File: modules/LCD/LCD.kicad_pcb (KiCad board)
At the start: 2 copper layers, 82.5 x 40.6 mm, 15 parts, among them J1 Conn_01x10_Male, J2 Conn_01x10_Male, J3 Conn_01x03_Male, J4 Conn_01x03_Male, U1 74LS139

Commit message: LCD. Fix hash.
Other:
- board text added: "e0b295"
- board text removed: "1c146a"

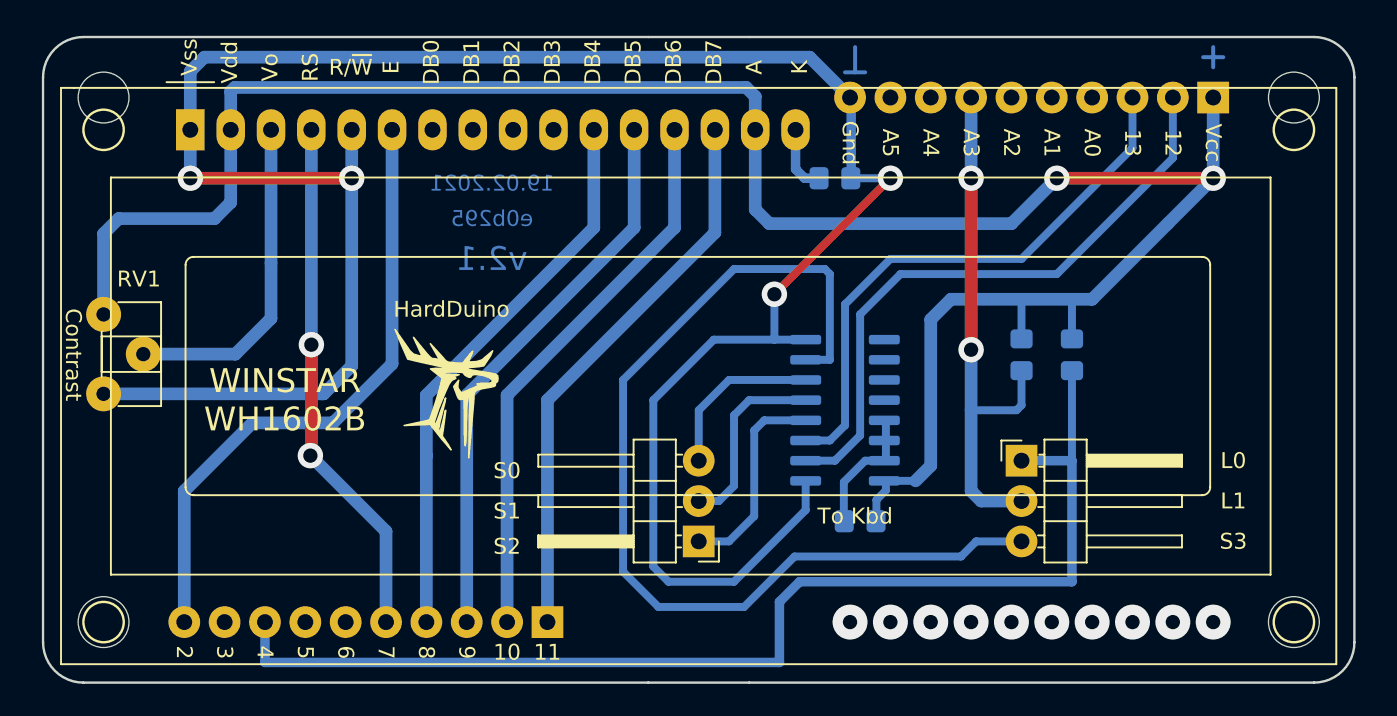
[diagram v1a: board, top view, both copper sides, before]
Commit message: LCD. Fix grid to 2.54, fix mounting holes position. This version is uncompatible with previous!!
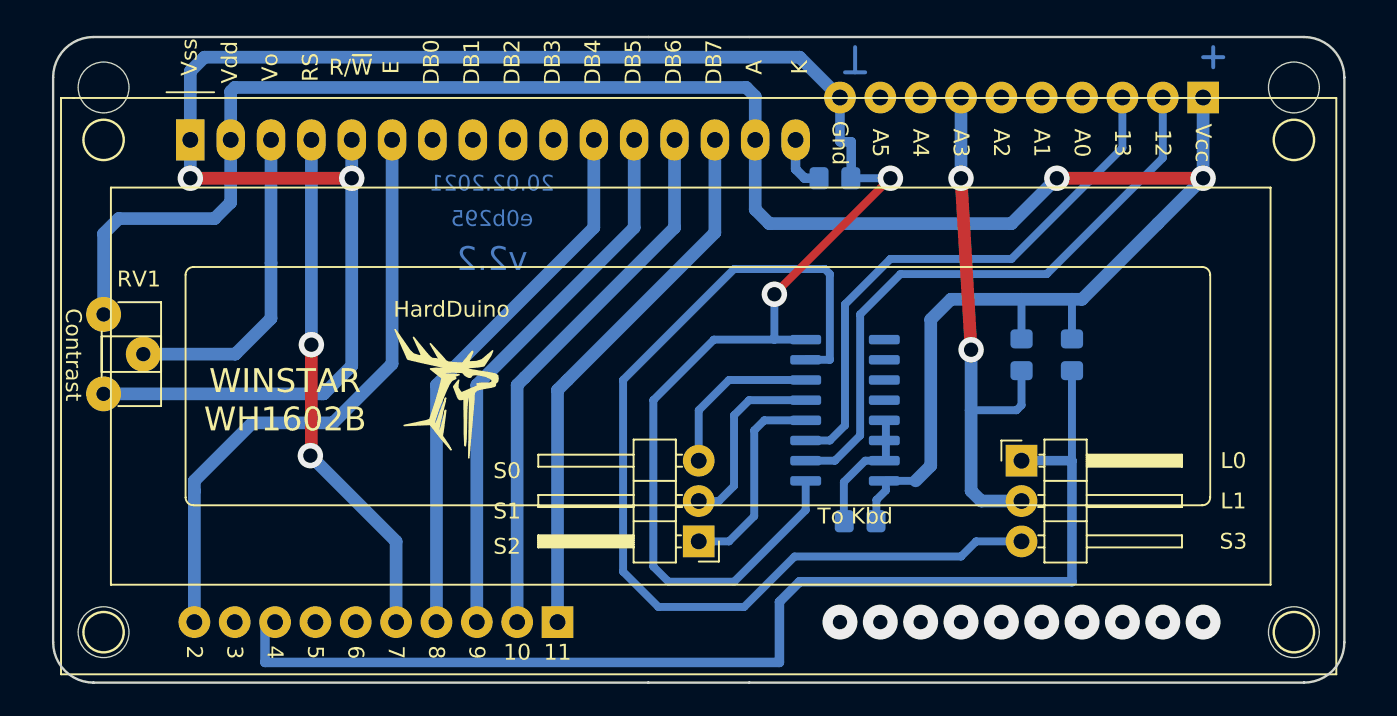
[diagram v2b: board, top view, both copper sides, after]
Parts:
- moved H1 0.64 mm to (148.0, 62.9)
- moved H3 0.64 mm to (73.0, 62.9)
- moved H2 0.64 mm to (148.0, 28.6)
- moved H4 0.64 mm to (73.0, 28.6)
- moved DS1 0.63 mm to (78.5, 31.9)
- moved J1 0.63 mm to (142.2, 29.2)
- moved J2 0.63 mm to (101.6, 62.2)
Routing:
- net VCC: track 138.5 -> 136.9 mm
- net /12: track 39.3 -> 38.6 mm
- net /13: track 35.8 -> 35.2 mm
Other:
- board size 82.5 x 40.6 mm -> 81.3 x 40.6 mm
- board text added: "20.02.2021"
- board text added: "v2.2"
- board text removed: "19.02.2021"
- board text removed: "v2.1"

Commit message: Now 2x shields have distance between 1x parts
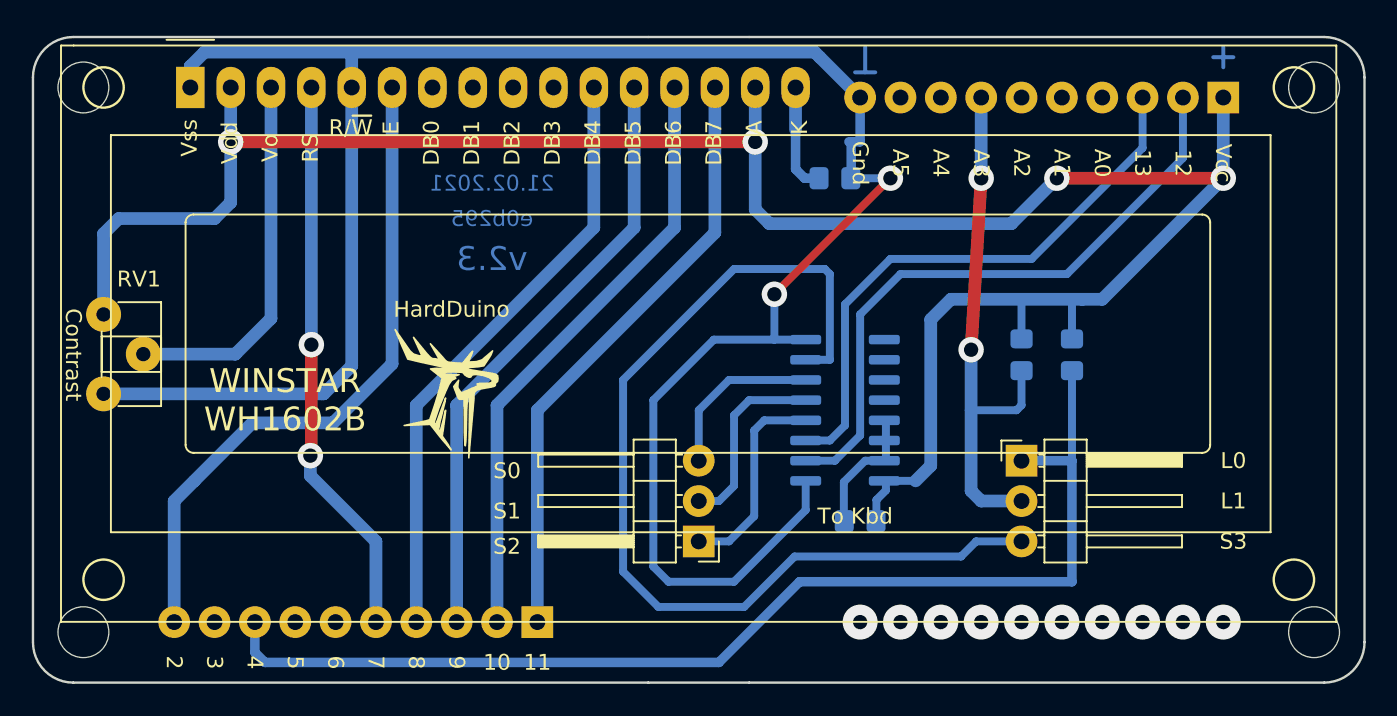
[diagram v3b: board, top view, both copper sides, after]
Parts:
- moved DS1 3.30 mm to (78.5, 28.6)
- moved H3 1.27 mm to (71.8, 62.9)
- moved H4 1.27 mm to (71.8, 28.6)
- moved J2 1.27 mm to (100.3, 62.2)
- moved H1 1.27 mm to (149.2, 62.9)
- moved H2 1.27 mm to (149.2, 28.6)
- moved J1 1.27 mm to (143.5, 29.2)
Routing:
- net GND: track 147.1 -> 139.2 mm, vias 4 -> 2
- net /8: track 35.1 -> 38.3 mm
- net /2: track 39.1 -> 42.3 mm
- net /11: track 35.1 -> 38.3 mm
- net /9: track 35.1 -> 38.3 mm
- net /10: track 35.1 -> 38.3 mm
- net VCC: track 136.9 -> 139.7 mm, vias 2 -> 4
- net Net-(DS1-Pad3): track 20.8 -> 23.5 mm
- net Net-(DS1-Pad16): track 4.16 -> 6.83 mm
- net /7: track 33.2 -> 35.4 mm
- net /4: track 74.1 -> 72.2 mm
- net /13: track 35.2 -> 36.5 mm
- net /12: track 38.6 -> 39.9 mm
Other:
- board size 81.3 x 40.6 mm -> 83.8 x 40.6 mm
- board text added: "21.02.2021"
- board text added: "v2.3"
- board text removed: "20.02.2021"
- board text removed: "v2.2"

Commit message: LCD. Pot was moved.
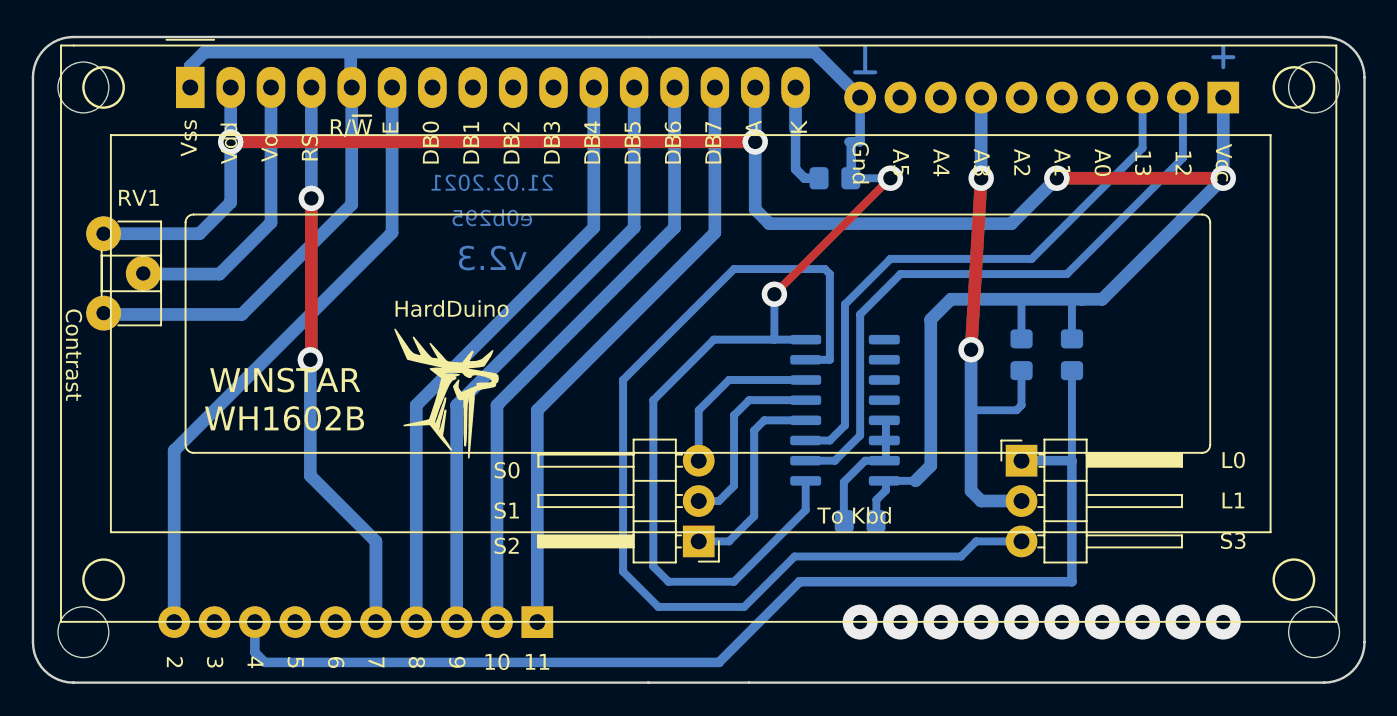
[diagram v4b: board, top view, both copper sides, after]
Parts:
- moved RV1 5.08 mm to (73.0, 37.8)
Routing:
- net GND: track 139.2 -> 131.2 mm
- net Net-(DS1-Pad3): track 23.5 -> 17.9 mm
- net VCC: track 139.7 -> 134.6 mm
- net /2: track 42.3 -> 39.3 mm

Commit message: Fix hash & version
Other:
- board text added: "b4d799"
- board text removed: "e0b295"
